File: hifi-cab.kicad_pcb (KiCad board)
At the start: 2 copper layers, 30 parts, among them J1 IR, J2 FAN 1, J3 FAN 2, J4 FAN 3, J5 DS18B20, J6 PWR IN, J7 RS-232, Q1 AO3400A, Q2 AO3400A, Q3 AO3400A, Q4 AO3400A, U1 TSR0.5-2433, U2 esp32-wemos-d1-mini

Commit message: Power routing complete
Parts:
- added REF**: MountingHole_2.2mm_M2_Pad_TopOnly, MountingHole:MountingHole_2.2mm_M2_Pad_TopOnly, F.Cu at (144.1, 138.2)
- added REF**: MountingHole_2.2mm_M2_Pad_TopOnly, MountingHole:MountingHole_2.2mm_M2_Pad_TopOnly, F.Cu at (144.1, 94.1)
- added REF**: MountingHole_2.2mm_M2_Pad_TopOnly, MountingHole:MountingHole_2.2mm_M2_Pad_TopOnly, F.Cu at (228.5, 138.2)
- moved R10 1.42 mm to (154.4, 104.4), turned to -90 degrees
- moved R11 1.35 mm to (167.5, 104.4), turned to -90 degrees
- moved R12 1.28 mm to (180.6, 104.3), turned to -90 degrees
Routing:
- net TACH3: track 8.48 -> 29.0 mm
- net TACH1: track 8.82 -> 28.3 mm, vias 0 -> 1
- net TACH2: track 8.48 -> 28.0 mm, vias 0 -> 1
- net RPM3: track 7.89 -> 19.6 mm, vias 1 -> 0
- net RPM1: track 7.89 -> 18.8 mm
- net RPM2: track 7.89 -> 18.6 mm
- net +3.3V: track 157.1 -> 158.8 mm, vias 0 -> 4
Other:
- board outline added: 90 x 50 mm
- board text added: "HIFI FAN PWM CONTROLLER CAMERON-MORGAN.COM V3.1"

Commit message: Start DRC
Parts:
- removed REF** (x3): MountingHole_2.2mm_M2_Pad_TopOnly, MountingHole:MountingHole_2.2mm_M2_Pad_TopOnly
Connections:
- U2 pad 10: unconnected-(U2-IO_19/D6-Pad10) -> FAN3_C
- U2 pad 11: DS18B20 -> TACH2
- U2 pad 12: RPM3 -> IR_C
- U2 pad 13: unconnected-(U2-IO_14/TMS-Pad13) -> RPM1
- U2 pad 18: unconnected-(U2-IO_13/TCK-Pad18) -> TACH1
- U2 pad 24: TACH3 -> unconnected-(U2-IO_27-Pad24)
- U2 pad 25: RPM2 -> unconnected-(U2-IO_22/D1/SCL-Pad25)
- U2 pad 26: TACH1 -> unconnected-(U2-IO_25-Pad26)
- U2 pad 27: RPM1 -> unconnected-(U2-IO_21/D2/SDA-Pad27)
- U2 pad 29: FAN1_C -> unconnected-(U2-IO_17/D3-Pad29)
- U2 pad 31: IR_C -> unconnected-(U2-IO_16/D4-Pad31)
- U2 pad 4: unconnected-(U2-IO_36/SVP/A0-Pad4) -> DS18B20
- U2 pad 5: unconnected-(U2-IO_39/SVN-Pad5) -> TACH3
- U2 pad 6: TACH2 -> FAN1_C
- U2 pad 7: FAN3_C -> RPM3
- U2 pad 9: unconnected-(U2-IO_33-Pad9) -> RPM2
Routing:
- net TACH1: track 28.3 -> 99.8 mm, vias 1 -> 3
- net IR_C: track 3.50 -> 49.8 mm
- net RPM1: track 18.8 -> 64.8 mm, vias 1 -> 3
- net FAN1_C: track 57.8 -> 96.7 mm
- net DS18B20: track 64.1 -> 102.8 mm
- net FAN2_C: track 43.2 -> 80.4 mm
- net FAN3_C: track 28.6 -> 64.0 mm
- net RPM2: track 18.6 -> 53.8 mm, vias 1 -> 3
- net TACH2: track 28.0 -> 63.0 mm, vias 1 -> 3
- net RPM3: track 19.6 -> 31.3 mm
- net TACH3: track 29.0 -> 40.4 mm
- net RX: track 79.5 -> 77.9 mm
- net +3.3V: track 158.8 -> 157.5 mm
- added copper zone on B.Cu, net GND

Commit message: Update hifi-cab.kicad_pcb
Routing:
- net RX: track 77.9 -> 79.0 mm
- net TX: track 75.1 -> 75.9 mm
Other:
- board text added: "IR LED CURRENT @ 3V"
- board text removed: "R9 IR LED CURRENT @ 3V"
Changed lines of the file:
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@@
 			(at 2.54 0 90)
 			(layer "F.SilkS")
+			(hide yes)
 			(effects
 				(font
@@
 			(at 2.54 1.92 90)
 			(layer "F.Fab")
+			(hide yes)
 			(effects
 				(font
@@
 		(layer "Edge.Cuts")
 	)
-	(gr_text "R9 IR LED\nCURRENT @ 3V"
-		(at 196.2 137.9 0)
+	(gr_text "IR LED\nCURRENT @ 3V"
+		(at 196.97 136.81 0)
 		(layer "F.SilkS")
 		(effects
@@
 				(bold yes)
 			)
+			(justify mirror)
 		)
 	)
@@
 				(bold yes)
 			)
+			(justify mirror)
 		)
 	)
@@
 				(bold yes)
 			)
+			(justify mirror)
 		)
 	)
@@
 				(bold yes)
 			)
+			(justify mirror)
 		)
 	)
@@
 				(bold yes)
 			)
+			(justify mirror)
 		)
 	)
@@
 				(bold yes)
 			)
+			(justify mirror)
 		)
 	)
@@
 				(bold yes)
 			)
+			(justify mirror)
 		)
 	)
@@
 				(bold yes)
 			)
+			(justify mirror)
 		)
 	)
@@
 	)
 	(segment
-		(start 185.36 117.31)
-		(end 192.621371 117.31)
+		(start 195.191371 114.74)
+		(end 199.96 114.74)
 		(width 0.2)
 		(layer "F.Cu")
@@
 	)
 	(segment
-		(start 195.191371 114.74)
-		(end 199.96 114.74)
+		(start 185.43 117.24)
+		(end 192.691371 117.24)
 		(width 0.2)
 		(layer "F.Cu")
@@
 	(segment
 		(start 184.17 118.5)
-		(end 185.36 117.31)
+		(end 185.43 117.24)
 		(width 0.2)
 		(layer "F.Cu")
@@
 	)
 	(segment
-		(start 192.621371 117.31)
+		(start 192.691371 117.24)
 		(end 195.191371 114.74)
 		(width 0.2)
@@
 	)
 	(segment
-		(start 204.3 133.3)
-		(end 171.2 133.3)
+		(start 221.95 99.5)
+		(end 217.817157 103.632843)
 		(width 0.2)
 		(layer "F.Cu")
@@
 	)
 	(segment
-		(start 217.817157 119.782843)
-		(end 204.3 133.3)
+		(start 204.3 133.3)
+		(end 171.2 133.3)
 		(width 0.2)
 		(layer "F.Cu")
@@
 	(segment
 		(start 223.8 99.5)
-		(end 217.817157 105.482843)
+		(end 221.95 99.5)
 		(width 0.2)
 		(layer "F.Cu")
@@
 	)
 	(segment
-		(start 217.817157 105.482843)
+		(start 217.817157 103.632843)
 		(end 217.817157 119.782843)
 		(width 0.2)
@@
 	)
 	(segment
-		(start 218.217157 107.182843)
-		(end 223.36 102.04)
+		(start 217.817157 119.782843)
+		(end 204.3 133.3)
 		(width 0.2)
 		(layer "F.Cu")
-		(net "TX")
+		(net "RX")
 	)
 	(segment
-		(start 173.3 133.7)
-		(end 204.5 133.7)
+		(start 204.5 133.7)
+		(end 218.217157 119.982843)
 		(width 0.2)
 		(layer "F.Cu")
@@
 	)
 	(segment
-		(start 223.36 102.04)
-		(end 225.36 102.04)
+		(start 218.217157 105.842843)
+		(end 222.02 102.04)
 		(width 0.2)
 		(layer "F.Cu")
@@
 	)
 	(segment
-		(start 218.217157 119.982843)
-		(end 218.217157 107.182843)
+		(start 171.6 135.4)
+		(end 173.3 133.7)
 		(width 0.2)
 		(layer "F.Cu")
@@
 	)
 	(segment
-		(start 171.6 135.4)
-		(end 173.3 133.7)
+		(start 222.02 102.04)
+		(end 225.36 102.04)
 		(width 0.2)
 		(layer "F.Cu")
@@
 	)
 	(segment
-		(start 204.5 133.7)
-		(end 218.217157 119.982843)
+		(start 173.3 133.7)
+		(end 204.5 133.7)
 		(width 0.2)
 		(layer "F.Cu")
@@
 	)
 	(segment
-		(start 173.2 112.3)
-		(end 173.2 116)
+		(start 218.217157 119.982843)
+		(end 218.217157 105.842843)
 		(width 0.2)
 		(layer "F.Cu")
-		(net "RPM2")
+		(net "TX")
 	)
 	(segment
@@
 	)
 	(segment
-		(start 196.8 109.66)
-		(end 199.96 109.66)
+		(start 173.2 112.3)
+		(end 173.2 116)
 		(width 0.2)
 		(layer "F.Cu")
@@
 	)
 	(segment
-		(start 192.75 116.05)
-		(end 196.04 112.76)
+		(start 187.95 116.05)
+		(end 192.07 116.05)
+		(width 0.2)
+		(layer "F.Cu")
+		(net "RPM2")
+	)
+	(segment
+		(start 196.04 112.08)
+		(end 196.04 110.42)
 		(width 0.2)
 		(layer "F.Cu")
@@
 	)
 	(segment
-		(start 187.95 116.05)
-		(end 192.75 116.05)
+		(start 192.07 116.05)
+		(end 196.04 112.08)
 		(width 0.2)
 		(layer "F.Cu")
@@
 	)
 	(segment
-		(start 196.04 112.76)
-		(end 196.04 110.42)
+		(start 196.8 109.66)
+		(end 199.96 109.66)
 		(width 0.2)
 		(layer "F.Cu")
@@
 	)
 	(segment
-		(start 183.27 117.5)
-		(end 183.86 116.91)
-		(width 0.2)
-		(layer "F.Cu")
-		(net "TACH2")
-	)
-	(segment
-		(start 192.455685 116.91)
-		(end 197.165685 112.2)
+		(start 192.31 116.75)
+		(end 196.86 112.2)
 		(width 0.2)
 		(layer "F.Cu")
@@
 	)
 	(segment
-		(start 183.86 116.91)
-		(end 192.455685 116.91)
+		(start 184.02 116.75)
+		(end 192.31 116.75)
 		(width 0.2)
 		(layer "F.Cu")
@@
 	)
 	(segment
-		(start 197.165685 112.2)
-		(end 199.96 112.2)
+		(start 167.52 95)
+		(end 167.52 103.48)
 		(width 0.2)
 		(layer "F.Cu")
@@
 	)
 	(segment
-		(start 167.52 95)
-		(end 167.52 103.48)
+		(start 183.27 117.5)
+		(end 184.02 116.75)
 		(width 0.2)
 		(layer "F.Cu")
@@
 		(width 0.2)
 		(layer "F.Cu")
+		(net "TACH2")
+	)
+	(segment
+		(start 196.86 112.2)
+		(end 199.96 112.2)
+		(width 0.2)
+		(layer "F.Cu")

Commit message: Ready for prod V3.1
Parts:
- added REF**: MountingHole_2.2mm_M2_Pad_TopOnly, MountingHole:MountingHole_2.2mm_M2_Pad_TopOnly, F.Cu at (229.0, 138.2)
- added REF**: MountingHole_2.2mm_M2_Pad_TopOnly, MountingHole:MountingHole_2.2mm_M2_Pad_TopOnly, F.Cu at (144.8, 138.2)
- added REF**: MountingHole_2.2mm_M2_Pad_TopOnly, MountingHole:MountingHole_2.2mm_M2_Pad_TopOnly, F.Cu at (144.8, 94.5)
- U2: value esp32-wemos-d1-mini -> mini ESP32
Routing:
- net RPM2: track 53.4 -> 52.4 mm
- net IR_C: track 49.8 -> 48.9 mm
- net FAN3_C: track 64.0 -> 63.4 mm
- net TX: track 75.9 -> 76.5 mm
- net DS18B20: track 102.8 -> 103.3 mm

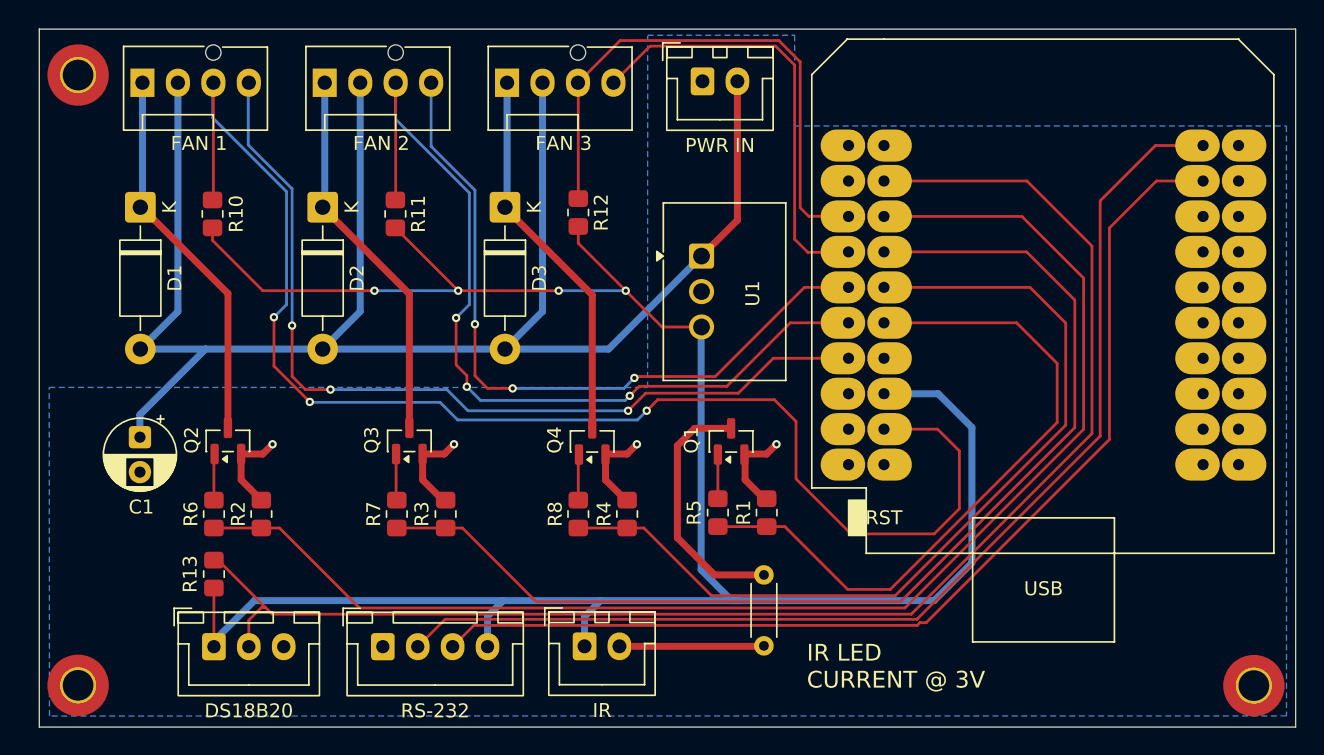
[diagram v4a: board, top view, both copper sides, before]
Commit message: Bump up 3.3V trace
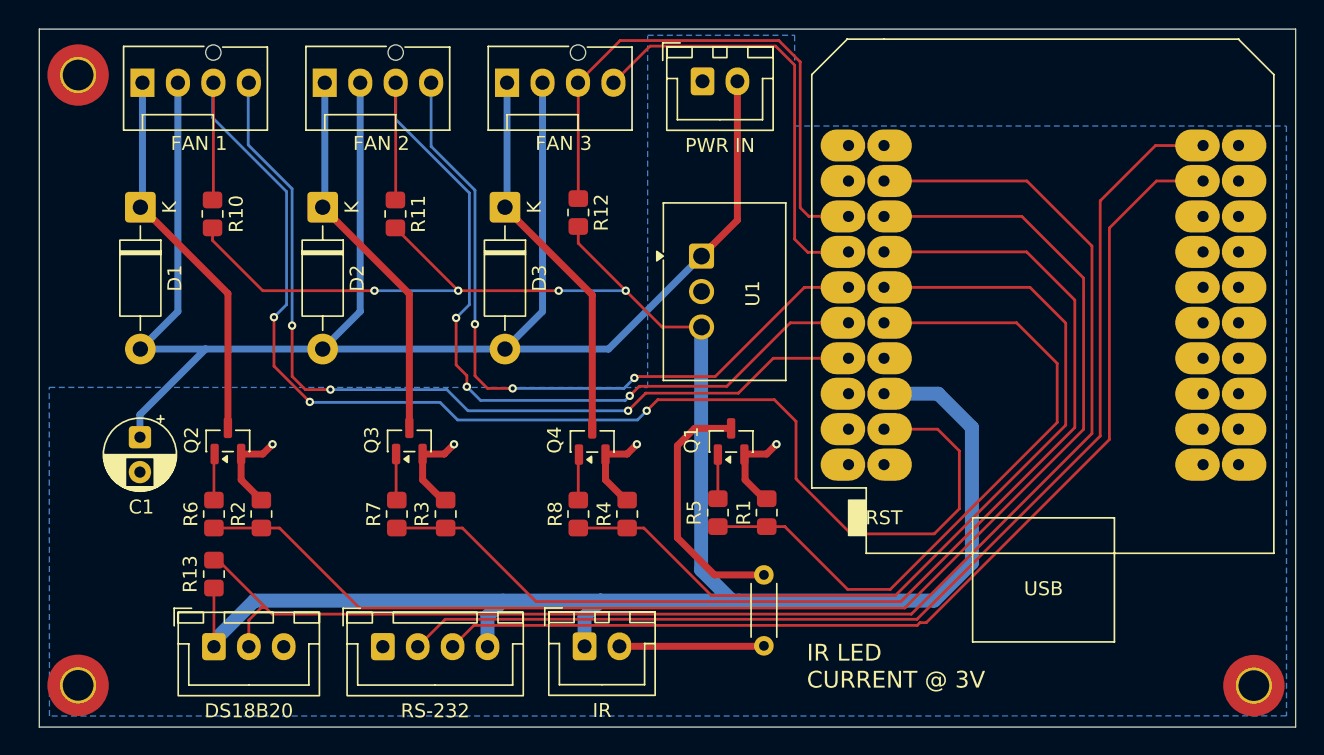
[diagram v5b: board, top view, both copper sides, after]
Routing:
- net +3.3V: track 157.5 -> 156.8 mm
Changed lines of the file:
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@@
 		(start 206.38 117.28)
 		(end 208.8 119.7)
-		(width 0.5)
+		(width 1)
+		(layer "B.Cu")
+		(net "+3.3V")
+	)
+	(segment
+		(start 157.4 132.1)
+		(end 154.5 135)
+		(width 1)
 		(layer "B.Cu")
 		(net "+3.3V")
@@
 		(start 174.1 135.4)
 		(end 174.1 133.225)
-		(width 0.5)
-		(layer "B.Cu")
-		(net "+3.3V")
-	)
-	(segment
-		(start 157.4 132.1)
-		(end 154 135.5)
-		(width 0.5)
+		(width 1)
 		(layer "B.Cu")
 		(net "+3.3V")
@@
 		(start 182.2 132.1)
 		(end 192.1 132.1)
-		(width 0.5)
+		(width 1)
 		(layer "B.Cu")
 		(net "+3.3V")
@@
 		(start 202.5 117.28)
 		(end 206.38 117.28)
-		(width 0.5)
+		(width 1)
+		(layer "B.Cu")
+		(net "+3.3V")
+	)
+	(segment
+		(start 182.2 132.1)
+		(end 157.4 132.1)
+		(width 1)
 		(layer "B.Cu")
 		(net "+3.3V")
@@
 		(start 189.4 112.53)
 		(end 189.4 129.9)
-		(width 0.5)
+		(width 1)
 		(layer "B.Cu")
 		(net "+3.3V")
@@
 		(start 192.1 132.1)
 		(end 206.1 132.1)
-		(width 0.5)
+		(width 1)
 		(layer "B.Cu")
 		(net "+3.3V")
@@
 		(start 174.1 133.225)
 		(end 175.225 132.1)
-		(width 0.5)
+		(width 1)
 		(layer "B.Cu")
 		(net "+3.3V")
@@
 		(start 208.8 129.4)
 		(end 206.1 132.1)
-		(width 0.5)
+		(width 1)
 		(layer "B.Cu")
 		(net "+3.3V")
@@
 		(start 189.4 129.9)
 		(end 191.6 132.1)
-		(width 0.5)
+		(width 1)
 		(layer "B.Cu")
 		(net "+3.3V")
@@
 		(start 181.05 135.375)
 		(end 181.05 133.25)
-		(width 0.5)
+		(width 1)
 		(layer "B.Cu")
 		(net "+3.3V")
@@
 		(start 181.05 133.25)
 		(end 182.2 132.1)
-		(width 0.5)
+		(width 1)
 		(layer "B.Cu")
 		(net "+3.3V")
@@
 		(start 208.8 119.7)
 		(end 208.8 129.4)
-		(width 0.5)
+		(width 1)
 		(layer "B.Cu")
 		(net "+3.3V")
-	)
-	(segment
-		(start 182.2 132.1)
-		(end 157.4 132.1)
-		(width 0.5)
-		(layer "B.Cu")
-		(net "+3.3V")

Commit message: Fix pin selection
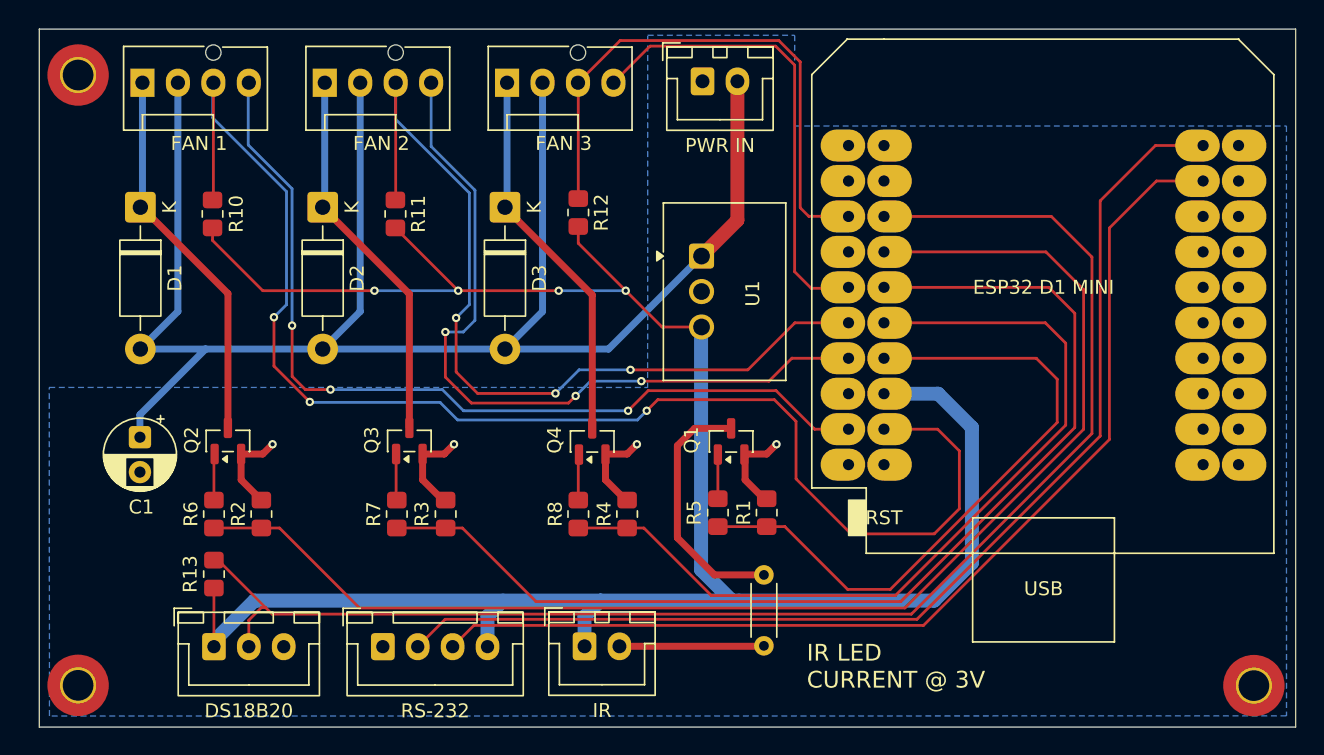
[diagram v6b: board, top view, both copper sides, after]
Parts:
- U2: value mini ESP32 -> ESP32 D1 MINI
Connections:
- J7 pad 2: RX -> TX
- J7 pad 3: TX -> RX
- U2 pad 10: FAN3_C -> FAN2_C
- U2 pad 12: IR_C -> FAN3_C
- U2 pad 13: RPM1 -> RPM2
- U2 pad 14: unconnected-(U2-IO_05/D8-Pad14) -> IR_C
- U2 pad 17: unconnected-(U2-IO_09/SD2-Pad17) -> RPM1
- U2 pad 21: RX -> TX
- U2 pad 23: TX -> RX
- U2 pad 4: DS18B20 -> unconnected-(U2-IO_36/SVP/A0-Pad4)
- U2 pad 6: FAN1_C -> DS18B20
- U2 pad 7: RPM3 -> unconnected-(U2-IO_35-Pad7)
- U2 pad 8: FAN2_C -> FAN1_C
- U2 pad 9: RPM2 -> RPM3
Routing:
- net TX: track 76.5 -> 79.4 mm
- net RX: track 79.4 -> 76.5 mm
- net RPM2: track 52.4 -> 55.0 mm
- net RPM3: track 31.3 -> 33.7 mm
- net FAN3_C: track 63.4 -> 61.5 mm
- net IR_C: track 48.9 -> 47.2 mm
- net FAN2_C: track 80.2 -> 78.5 mm
- net FAN1_C: track 96.8 -> 95.3 mm
- net DS18B20: track 103.3 -> 101.8 mm
- net TACH2: track 63.2 -> 62.6 mm

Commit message: Change C1 footprint
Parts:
- removed REF** (x3): MountingHole_2.2mm_M2_Pad_TopOnly, MountingHole:MountingHole_2.2mm_M2_Pad_TopOnly
- added C2: 100nF, Capacitor_SMD:C_0805_2012Metric_Pad1.18x1.45mm_HandSolder, F.Cu at (189.8, 137.7)
- C1: footprint Capacitor_THT:CP_Radial_D5.0mm_P2.50mm -> Capacitor_THT:CP_Radial_D6.3mm_P2.50mm
- U2: value ESP32 D1 MINI -> esp32-wemos-d1-mini
- moved C1 1.57 mm to (147.6, 120.5)
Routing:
- net +3.3V: track 156.8 -> 165.4 mm
- net Net-(J1-Pin_2): track 10.3 -> 14.4 mm

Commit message: Update hifi-cab.kicad_pcb
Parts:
- U2: value esp32-wemos-d1-mini -> ESP32 D1 MINI
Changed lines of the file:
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@@
 			)
 		)
-		(property "Value" "esp32-wemos-d1-mini"
+		(property "Value" "ESP32 D1 MINI"
 			(at 0 -1.27 0)
 			(layer "F.SilkS")
